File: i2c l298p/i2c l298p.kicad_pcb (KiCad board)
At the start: 2 copper layers, 123.2 x 50.2 mm, 81 parts, among them J1 power in, J10 Conn_01x01, J2 Conn_01x04, J3 Conn_01x04, J4 Conn_01x04, J5 Conn_01x04, J6 to qwiic breakout, J7 qwiic 1, J8 qwiic 2, J9 qwiic 2, U1 ILQ620GB-X009, U2 ILQ620GB-X009, U3 ILQ620GB-X009, U4 ILQ620GB-X009, U5 PCA9685PW

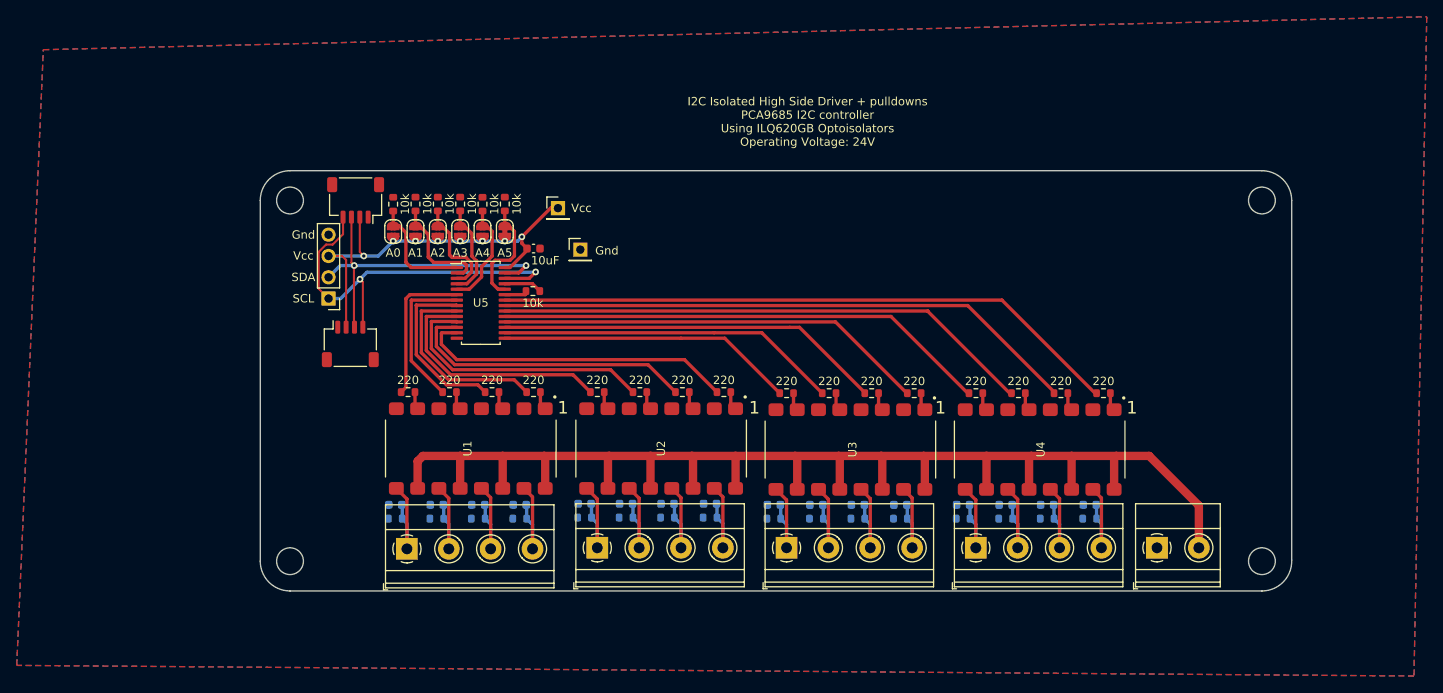
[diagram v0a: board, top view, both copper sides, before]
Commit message: finished motor controller layout
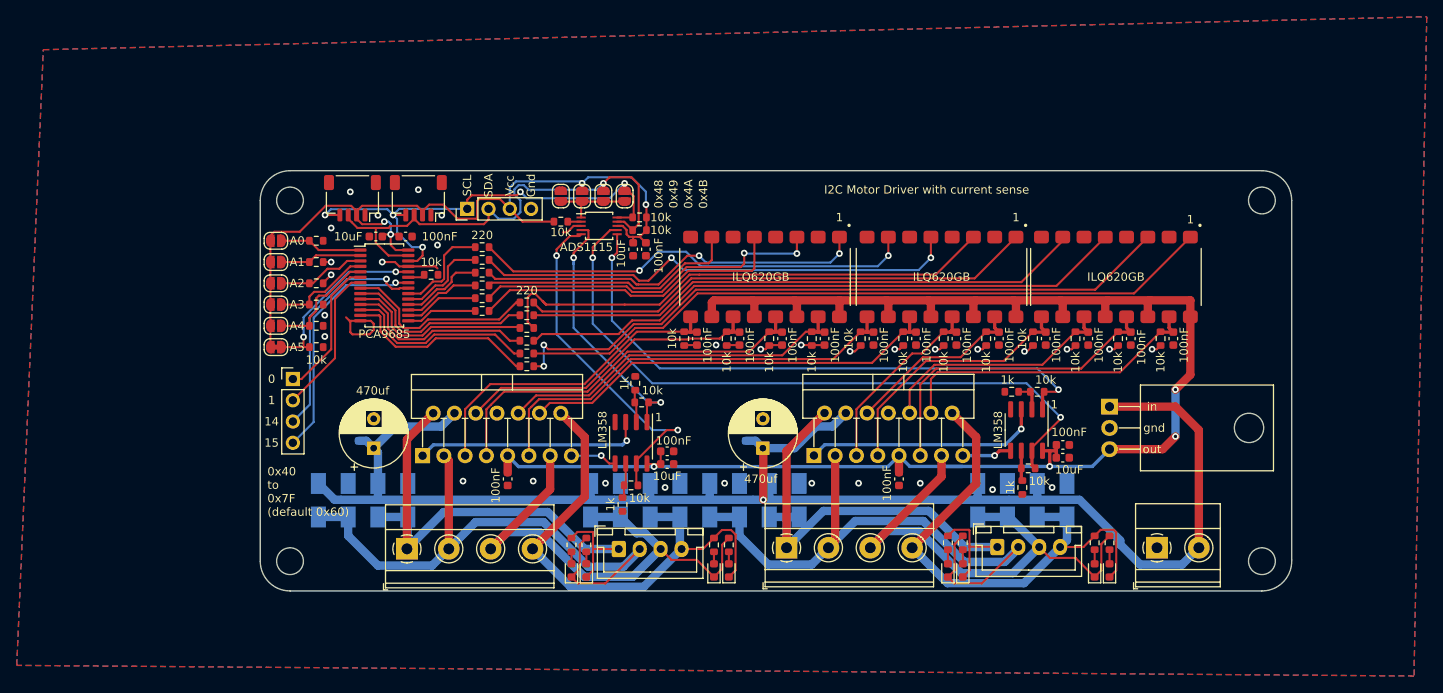
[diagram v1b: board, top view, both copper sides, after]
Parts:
- removed J10: Conn_01x01, Connector_PinHeader_2.54mm:PinHeader_1x01_P2.54mm_Vertical
- added C18: 470uf, Capacitor_THT:CP_Radial_D8.0mm_P3.50mm, F.Cu at (104.4, 113.4)
- added C19: 100nF, Capacitor_SMD:C_0603_1608Metric, F.Cu at (120.4, 117.1)
- added C20: 100nF, Capacitor_SMD:C_0603_1608Metric, F.Cu at (108.2, 88.1)
- added C21: 10uF, Capacitor_SMD:C_0603_1608Metric, F.Cu at (135.4, 89.7)
- added C22: 100nF, Capacitor_SMD:C_0603_1608Metric, F.Cu at (136.9, 89.7)
- added C23: 10uF, Capacitor_SMD:C_0603_1608Metric, F.Cu at (139.4, 115.3)
- added C24: 10uF, Capacitor_SMD:C_0603_1608Metric, F.Cu at (186.7, 114.6)
- added C25: 100nF, Capacitor_SMD:C_0603_1608Metric, F.Cu at (139.4, 113.8)
- added C26: 100nF, Capacitor_SMD:C_0603_1608Metric, F.Cu at (186.7, 113.0)
- added D1: DIODE, Diode_SMD:D_SMA, B.Cu at (151.6, 119.6)
- added D10: DIODE, Diode_SMD:D_SMA, B.Cu at (180.1, 119.6)
- added D11: DIODE, Diode_SMD:D_SMA, B.Cu at (130.3, 119.6)
- added D12: DIODE, Diode_SMD:D_SMA, B.Cu at (133.9, 119.6)
- added D13: DIODE, Diode_SMD:D_SMA, B.Cu at (183.6, 119.6)
- added D14: DIODE, Diode_SMD:D_SMA, B.Cu at (187.2, 119.6)
- added D15: DIODE, Diode_SMD:D_SMA, B.Cu at (137.4, 119.6)
- added D16: DIODE, Diode_SMD:D_SMA, B.Cu at (141.0, 119.6)
- added D17: LED, LED_SMD:LED_0603_1608Metric, F.Cu at (173.0, 128.0)
- added D18: LED, LED_SMD:LED_0603_1608Metric, F.Cu at (192.3, 128.0)
- added D19: LED, LED_SMD:LED_0603_1608Metric, F.Cu at (128.0, 128.0)
- added D2: DIODE, Diode_SMD:D_SMA, B.Cu at (155.2, 119.6)
- added D20: LED, LED_SMD:LED_0603_1608Metric, F.Cu at (146.8, 128.0)
- added D21: LED, LED_SMD:LED_0603_1608Metric, F.Cu at (174.8, 128.0)
- added D22: LED, LED_SMD:LED_0603_1608Metric, F.Cu at (190.5, 128.0)
- added D23: LED, LED_SMD:LED_0603_1608Metric, F.Cu at (129.8, 128.0)
- added D24: LED, LED_SMD:LED_0603_1608Metric, F.Cu at (145.0, 128.0)
- added D3: DIODE, Diode_SMD:D_SMA, B.Cu at (104.9, 119.6)
- added D4: DIODE, Diode_SMD:D_SMA, B.Cu at (108.5, 119.6)
- added D5: DIODE, Diode_SMD:D_SMA, B.Cu at (144.5, 119.6)
- added D6: DIODE, Diode_SMD:D_SMA, B.Cu at (148.1, 119.6)
- added D7: DIODE, Diode_SMD:D_SMA, B.Cu at (97.8, 119.6)
- added D8: DIODE, Diode_SMD:D_SMA, B.Cu at (101.3, 119.6)
- added D9: DIODE, Diode_SMD:D_SMA, B.Cu at (176.5, 119.6)
- added JP10: Jumper_2_Open, Jumper:SolderJumper-2_P1.3mm_Open_RoundedPad1.0x1.5mm, F.Cu at (126.7, 83.3)
- added JP7: Jumper_2_Open, Jumper:SolderJumper-2_P1.3mm_Open_RoundedPad1.0x1.5mm, F.Cu at (134.4, 83.3)
- added JP8: Jumper_2_Open, Jumper:SolderJumper-2_P1.3mm_Open_RoundedPad1.0x1.5mm, F.Cu at (131.8, 83.3)
- added JP9: Jumper_2_Open, Jumper:SolderJumper-2_P1.3mm_Open_RoundedPad1.0x1.5mm, F.Cu at (129.3, 83.3)
- added R40: 1k, Resistor_SMD:R_0603_1608Metric, F.Cu at (174.8, 124.7)
- added R41: 1k, Resistor_SMD:R_0603_1608Metric, F.Cu at (190.5, 124.7)
- added R42: 1k, Resistor_SMD:R_0603_1608Metric, F.Cu at (129.8, 125.0)
- added R43: 1k, Resistor_SMD:R_0603_1608Metric, F.Cu at (145.0, 125.0)
- added R44: 10k, Resistor_SMD:R_0603_1608Metric, F.Cu at (126.7, 86.4)
- added R45: 10k, Resistor_SMD:R_0603_1608Metric, F.Cu at (136.1, 85.9)
- added R46: 10k, Resistor_SMD:R_0603_1608Metric, F.Cu at (136.1, 87.4)
- added R47: 1k, Resistor_SMD:R_0603_1608Metric, F.Cu at (135.6, 105.7)
- added R48: 1k, Resistor_SMD:R_0603_1608Metric, F.Cu at (134.1, 120.1)
- added R49: 1k, Resistor_SMD:R_0603_1608Metric, F.Cu at (180.6, 106.7)
- added R50: 1k, Resistor_SMD:R_0603_1608Metric, F.Cu at (181.9, 118.1)
- added U10: LM358, Package_SO:SOIC-8_3.9x4.9mm_P1.27mm, F.Cu at (182.4, 111.3)
- added U6: L298HN, Package_TO_SOT_THT:TO-220-15_P2.54x2.54mm_StaggerOdd_Lead4.58mm_Vertical, F.Cu at (110.2, 114.3)
- added U7: L7805, Package_TO_SOT_THT:TO-220-3_Horizontal_TabDown, F.Cu at (192.3, 108.5)
- added U8: ADS1115, Package_SO:TSSOP-10_3x3mm_P0.5mm, F.Cu at (131.3, 86.9)
- added U9: LM358, Package_SO:SOIC-8_3.9x4.9mm_P1.27mm, F.Cu at (135.1, 112.8)
- C1, C10, C11, C12, C13, C2, C3, C4, C5, C6, C7, C8, C9, R17, R18, R19, R20, R21, R22, R23, R24, R25, R26, R27, R28: moved to F.Cu
- C16: value 100nF -> 470uf; footprint Capacitor_SMD:C_0603_1608Metric -> Capacitor_THT:CP_Radial_D8.0mm_P3.50mm; moved to F.Cu
- J3, J5: value Conn_01x04 -> jst; footprint TerminalBlock_Phoenix:TerminalBlock_Phoenix_MKDS-1,5-4_1x04_P5.00mm_Horizontal -> Connector_JST:JST_XH_B4B-XH-A_1x04_P2.50mm_Vertical
- J9: value qwiic 2 -> extra pwm; footprint Connector_PinHeader_2.54mm:PinHeader_1x01_P2.54mm_Vertical -> Connector_PinHeader_2.54mm:PinHeader_1x04_P2.54mm_Vertical
- R13, R14, R15, R16: value 220 -> 10k
- R29, R30, R31, R32: value 10k -> 1k; moved to F.Cu
- U1, U2, U3: value ILQ620GB-X009 -> ILQ620GB
- U4: value ILQ620GB-X009 -> L298HN; footprint Evan's misc parts:OPTO_ILQ620GB-X009 -> Package_TO_SOT_THT:TO-220-15_P2.54x2.54mm_StaggerOdd_Lead4.58mm_Vertical
- U5: value PCA9685PW -> PCA9685
- moved C15 82.6 mm to (102.6, 111.8), turned to 90 degrees
- moved C2 75.4 mm to (184.7, 100.3), turned to -90 degrees
- moved C1 74.8 mm to (179.1, 100.3), turned to -90 degrees
- moved R18 74.4 mm to (183.1, 100.3), turned to -90 degrees
- moved R17 73.8 mm to (177.5, 100.3), turned to -90 degrees
- moved C5 73.0 mm to (199.9, 100.3), turned to -90 degrees
- moved R21 72.0 mm to (198.4, 100.3), turned to -90 degrees
- moved C4 70.7 mm to (189.7, 100.3), turned to -90 degrees
- moved R20 69.8 mm to (188.2, 100.3), turned to -90 degrees
- moved C6 63.4 mm to (194.8, 100.3), turned to -90 degrees
- moved R22 62.5 mm to (193.3, 100.3), turned to -90 degrees
- moved C3 60.5 mm to (174.0, 100.3), turned to -90 degrees
- moved R19 59.6 mm to (172.5, 100.3), turned to -90 degrees
- moved U2 58.1 mm to (193.0, 93.0)
- moved R31 56.9 mm to (128.0, 125.0), turned to -90 degrees
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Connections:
- C1 pad 1: Net-(C1-Pad1) -> m2 pwm
- C10 pad 1: Net-(C10-Pad1) -> m1 in1
- C11 pad 1: Net-(C11-Pad1) -> m1 in2
- C12 pad 1: Net-(C12-Pad1) -> m1 pwm
- C13 pad 1: Net-(C13-Pad1) -> +5V
- C14 pad 1: Net-(C14-Pad1) -> +24V
- C15 pad 1: Net-(C15-Pad1) -> +24V
- C16 pad 1: Net-(C16-Pad1) -> +24V
- C2 pad 1: Net-(C2-Pad1) -> m2 in2
- C3 pad 1: Net-(C3-Pad1) -> m2 in1
- C4 pad 1: Net-(C4-Pad1) -> m3 in1
- C5 pad 1: Net-(C5-Pad1) -> m3 in2
- C6 pad 1: Net-(C6-Pad1) -> m3 pwm
- C7 pad 1: Net-(C7-Pad1) -> m0 pwm
- C8 pad 1: Net-(C8-Pad1) -> m0 in2
- C9 pad 1: Net-(C9-Pad1) -> m0 in1
- J2 pad 1: Net-(C1-Pad1) -> Net-(J2-Pad1)
- J2 pad 2: Net-(C2-Pad1) -> Net-(J2-Pad2)
- J2 pad 3: Net-(C3-Pad1) -> Net-(J2-Pad3)
- J2 pad 4: Net-(C4-Pad1) -> Net-(J2-Pad4)
- J3 pad 1: Net-(C5-Pad1) -> Net-(J4-Pad1)
- J3 pad 2: Net-(C6-Pad1) -> Net-(J4-Pad2)
- J3 pad 3: Net-(C7-Pad1) -> Net-(J4-Pad3)
- J3 pad 4: Net-(C8-Pad1) -> Net-(J4-Pad4)
- J4 pad 1: Net-(C9-Pad1) -> Net-(J4-Pad1)
- J4 pad 2: Net-(C10-Pad1) -> Net-(J4-Pad2)
- J4 pad 3: Net-(C11-Pad1) -> Net-(J4-Pad3)
- J4 pad 4: Net-(C12-Pad1) -> Net-(J4-Pad4)
- J5 pad 1: Net-(C13-Pad1) -> Net-(J2-Pad1)
- J5 pad 2: Net-(C14-Pad1) -> Net-(J2-Pad2)
- J5 pad 3: Net-(C15-Pad1) -> Net-(J2-Pad3)
- J5 pad 4: Net-(C16-Pad1) -> Net-(J2-Pad4)
- J7 pad MP: (no net) -> GND
- J8 pad MP: (no net) -> GND
- J9 pad 1: VCC -> /pwm0
- R1 pad 1: Net-(R1-Pad1) -> Net-(U3-Pad1)
- R1 pad 2: /pwm0 -> /pwm2
- R10 pad 2: /pwm9 -> /pwm11
- R11 pad 1: Net-(R11-Pad1) -> Net-(U3-Pad5)
- R11 pad 2: /pwm10 -> /pwm12
- R12 pad 2: /pwm11 -> /pwm13
- R13 pad 1: Net-(R13-Pad1) -> m1 pwm
- R13 pad 2: /pwm12 -> GND
- R14 pad 1: Net-(R14-Pad1) -> sense 0
- R14 pad 2: /pwm13 -> Net-(R14-Pad2)
- R15 pad 1: Net-(R15-Pad1) -> sense 1
- R15 pad 2: /pwm14 -> Net-(R15-Pad2)
- R16 pad 1: Net-(R16-Pad1) -> sense 2
- R16 pad 2: /pwm15 -> Net-(R16-Pad2)
- R17 pad 1: Net-(C1-Pad1) -> m2 pwm
- R18 pad 1: Net-(C2-Pad1) -> m2 in2
- R19 pad 1: Net-(C3-Pad1) -> m2 in1
- R2 pad 2: /pwm1 -> /pwm3
- R20 pad 1: Net-(C4-Pad1) -> m3 in1
- R21 pad 1: Net-(C5-Pad1) -> m3 in2
- R22 pad 1: Net-(C6-Pad1) -> m3 pwm
- R23 pad 1: Net-(C7-Pad1) -> m0 pwm
- R24 pad 1: Net-(C8-Pad1) -> m0 in2
- R25 pad 1: Net-(C9-Pad1) -> m0 in1
- R26 pad 1: Net-(C10-Pad1) -> m1 in1
- R27 pad 1: Net-(C11-Pad1) -> m1 in2
- R28 pad 1: Net-(C12-Pad1) -> sense 3
- R28 pad 2: GND -> Net-(R28-Pad2)
- R29 pad 1: Net-(C13-Pad1) -> Net-(J4-Pad1)
- R29 pad 2: GND -> Net-(D17-Pad2)
- R3 pad 1: Net-(R3-Pad1) -> Net-(U3-Pad3)
- R3 pad 2: /pwm2 -> /pwm4
- R30 pad 1: Net-(C14-Pad1) -> Net-(J4-Pad3)
- R30 pad 2: GND -> Net-(D18-Pad2)
- R31 pad 1: Net-(C15-Pad1) -> Net-(J2-Pad1)
- R31 pad 2: GND -> Net-(D19-Pad2)
- R32 pad 1: Net-(C16-Pad1) -> Net-(J2-Pad3)
- R32 pad 2: GND -> Net-(D20-Pad2)
- R4 pad 1: Net-(R4-Pad1) -> Net-(U2-Pad5)
- R4 pad 2: /pwm3 -> /pwm5
- R5 pad 1: Net-(R5-Pad1) -> Net-(U2-Pad1)
- R5 pad 2: /pwm4 -> /pwm6
- R6 pad 2: /pwm5 -> /pwm7
- R7 pad 1: Net-(R7-Pad1) -> Net-(U1-Pad5)
- R7 pad 2: /pwm6 -> /pwm8
- R8 pad 2: /pwm7 -> /pwm9
- R9 pad 2: /pwm8 -> /pwm10
- U1 pad 1: Net-(R4-Pad1) -> Net-(R10-Pad1)
- U1 pad 10: +24V -> +5V
- U1 pad 11: Net-(C2-Pad1) -> m0 pwm
- U1 pad 12: +24V -> +5V
- U1 pad 13: Net-(C3-Pad1) -> m0 in2
- U1 pad 14: +24V -> +5V
- U1 pad 15: Net-(C4-Pad1) -> m1 in1
- U1 pad 16: +24V -> +5V
- U1 pad 3: Net-(R3-Pad1) -> Net-(R8-Pad1)
- U1 pad 5: Net-(R2-Pad1) -> Net-(U1-Pad5)
- U1 pad 7: Net-(R1-Pad1) -> Net-(R9-Pad1)
- U1 pad 9: Net-(C1-Pad1) -> m0 in1
- U2 pad 1: Net-(R8-Pad1) -> Net-(U2-Pad1)
- U2 pad 10: +24V -> +5V
- U2 pad 11: Net-(C6-Pad1) -> m3 in1
- U2 pad 12: +24V -> +5V
- U2 pad 13: Net-(C7-Pad1) -> m3 pwm
- U2 pad 14: +24V -> +5V
- U2 pad 15: Net-(C8-Pad1) -> m3 in2
- U2 pad 16: +24V -> +5V
- U2 pad 3: Net-(R7-Pad1) -> Net-(R6-Pad1)
- U2 pad 5: Net-(R6-Pad1) -> Net-(U2-Pad5)
- U2 pad 7: Net-(R5-Pad1) -> Net-(R2-Pad1)
- U2 pad 9: Net-(C5-Pad1) -> m2 in2
- U3 pad 1: Net-(R12-Pad1) -> Net-(U3-Pad1)
- U3 pad 10: +24V -> +5V
- U3 pad 11: Net-(C10-Pad1) -> m1 in2
- U3 pad 12: +24V -> +5V
- U3 pad 13: Net-(C11-Pad1) -> m2 in1
- U3 pad 14: +24V -> +5V
- U3 pad 15: Net-(C12-Pad1) -> m2 pwm
- U3 pad 16: +24V -> +5V
- U3 pad 3: Net-(R11-Pad1) -> Net-(U3-Pad3)
- U3 pad 5: Net-(R10-Pad1) -> Net-(U3-Pad5)
- U3 pad 7: Net-(R9-Pad1) -> Net-(R12-Pad1)
- U3 pad 9: Net-(C9-Pad1) -> m1 pwm
- U4 pad 1: Net-(R16-Pad1) -> Net-(U4-Pad1)
- U4 pad 10: +24V -> m3 in1
- U4 pad 11: Net-(C14-Pad1) -> m3 pwm
- U4 pad 12: +24V -> m3 in2
- U4 pad 13: Net-(C15-Pad1) -> Net-(J4-Pad3)
- U4 pad 14: +24V -> Net-(J4-Pad4)
- U4 pad 15: Net-(C16-Pad1) -> Net-(U4-Pad15)
- U4 pad 2: GND -> Net-(J4-Pad1)
- U4 pad 3: Net-(R15-Pad1) -> Net-(J4-Pad2)
- U4 pad 4: GND -> +24V
- U4 pad 5: Net-(R14-Pad1) -> m2 in1
- U4 pad 6: GND -> m2 pwm
- U4 pad 7: Net-(R13-Pad1) -> m2 in2
- U4 pad 9: Net-(C13-Pad1) -> +5V
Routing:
- net +5V: track 0.00 -> 204.6 mm, vias 0 -> 4
- net Net-(U2-Pad1): track 0.00 -> 84.2 mm
- net sense 3: track 0.00 -> 81.1 mm, vias 0 -> 2
- net Net-(R6-Pad1): track 2.17 -> 81.6 mm, vias 0 -> 2
- net Net-(J2-Pad2): track 0.00 -> 74.4 mm
- net Net-(U2-Pad5): track 0.00 -> 73.4 mm
- net Net-(J4-Pad2): track 0.00 -> 73.0 mm
- net sense 2: track 0.00 -> 71.3 mm, vias 0 -> 2
- net Net-(J4-Pad1): track 0.00 -> 66.2 mm
- net Net-(J2-Pad1): track 0.00 -> 65.5 mm
- net Net-(R2-Pad1): track 2.17 -> 67.3 mm
- net Net-(J4-Pad4): track 0.00 -> 62.5 mm
- net Net-(J2-Pad4): track 0.00 -> 62.0 mm
- net Net-(J2-Pad3): track 0.00 -> 61.9 mm
- net Net-(U3-Pad3): track 0.00 -> 61.8 mm
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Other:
- board text added: "0x40 to 0x7F (default 0x60)"
- board text added: "0x48"
- board text added: "0x49"
- board text added: "0x4A"
- board text added: "0x4B"
- board text added: "10k"
- board text added: "I2C L298 motor driver PCA9685 I2C controller Using ILQ620GB Optoisolators ADS1115 for current sense Operating Voltage: up to 24V (5v regulator limits)"
- board text added: "I2C Motor Driver with current sense"
- board text added: "M1+"
- board text added: "M1-"
- board text added: "M2+"
- board text added: "M2-"
- board text added: "M3+"
- board text added: "M3-"
- board text added: "M4+"
- board text added: "M4-"
- board text added: "gnd"
- board text added: "in"
- board text added: "out"
- board text removed: "10"
- board text removed: "11"
- board text removed: "12"
- board text removed: "13"
- board text removed: "2"
- board text removed: "3"
- board text removed: "4"
- board text removed: "5"
- board text removed: "6"
- board text removed: "7"
- board text removed: "8"
- board text removed: "9"
- board text removed: "I2C Isolated High Side Driver + pulldowns PCA9685 I2C controller Using ILQ620GB Optoisolators Operating Voltage: 24V"
- board text removed: "This has 10K pulldowns, so it will not work to drive things hard low"

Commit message: generated gerbers
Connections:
- J7 pad MP: GND -> (no net)
- J8 pad MP: GND -> (no net)
